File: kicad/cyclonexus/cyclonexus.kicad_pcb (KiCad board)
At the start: 2 copper layers, 92.7 x 111.8 mm, 22 parts, among them CON1 BARREL_JACK, CON2 BARREL_JACK, J1 RJ14, J10 RJ14, J11 RJ14, J12 RJ14, J13 RJ14, J14 RJ14, J15 RJ14, J16 RJ14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

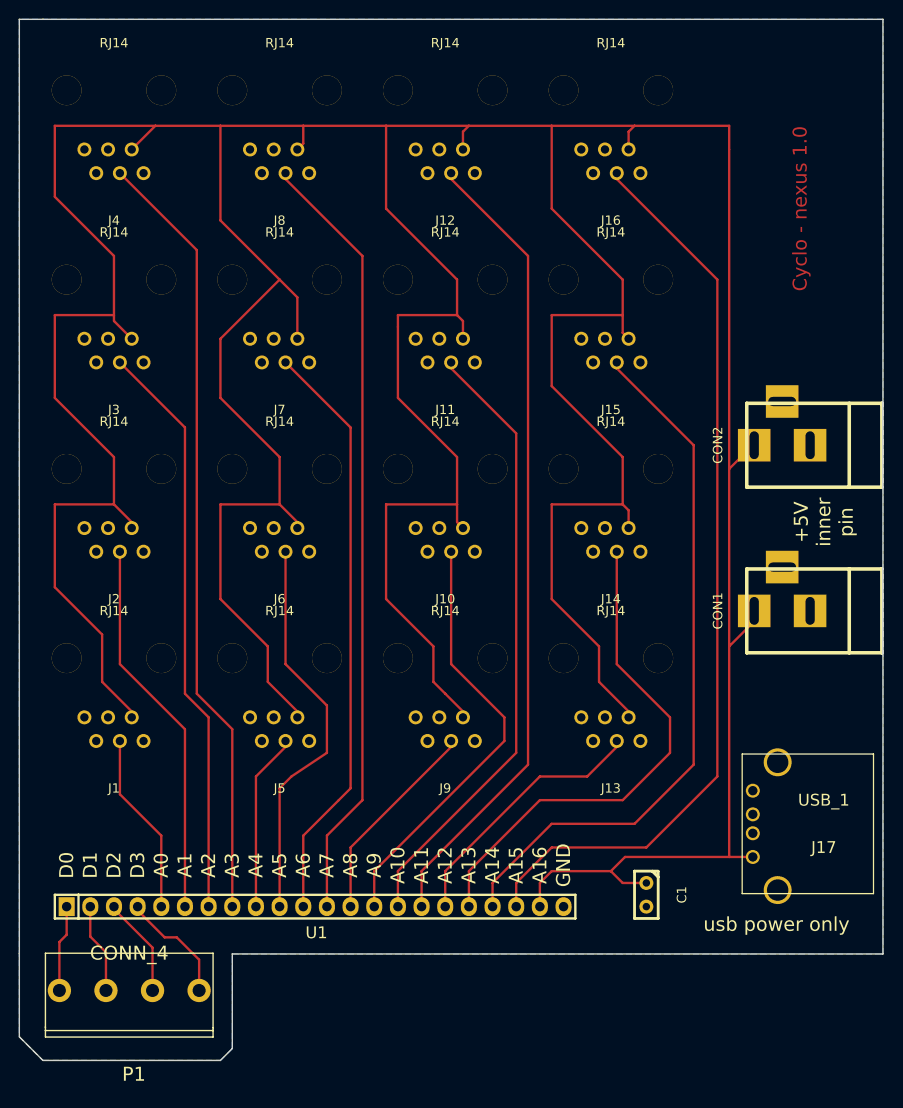
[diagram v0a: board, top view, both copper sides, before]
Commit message: add mounting holes
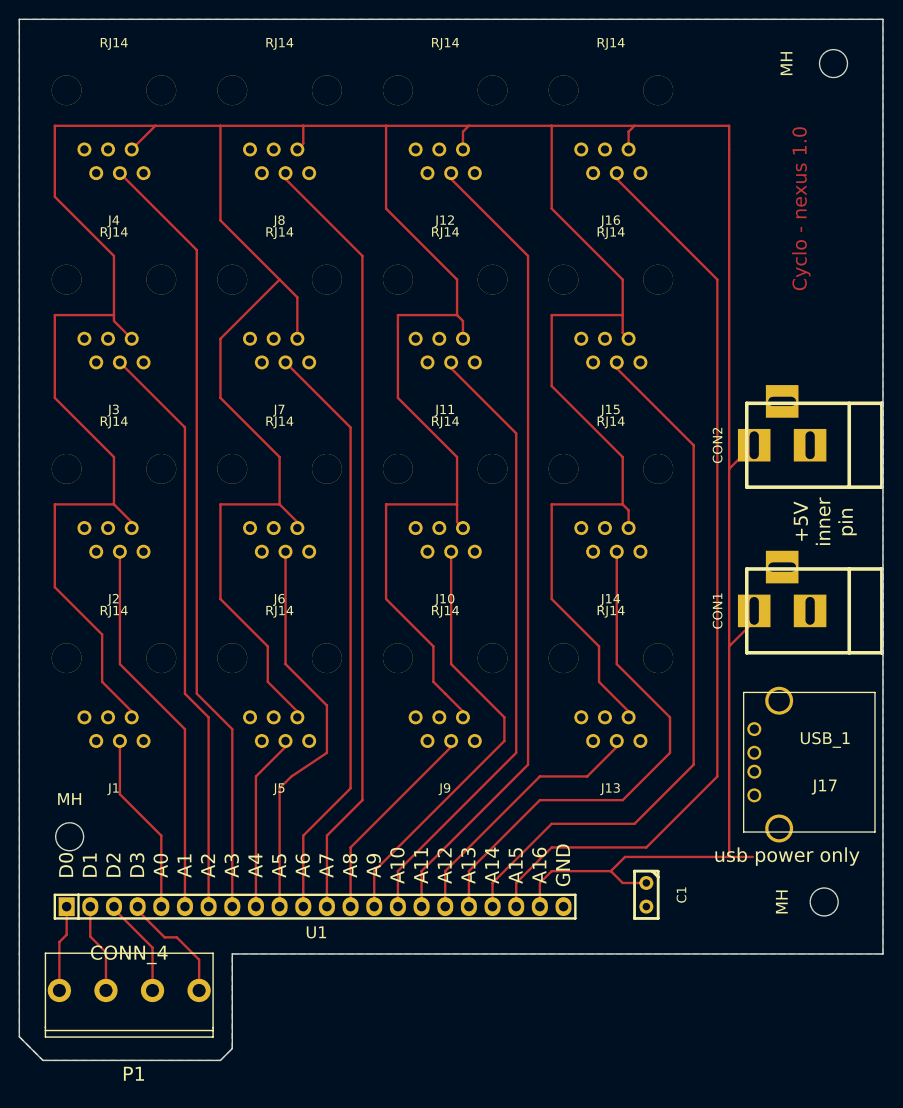
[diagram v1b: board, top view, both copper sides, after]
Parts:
- added MH: MountingHole_3mm_RevA_Date21Jun2010, Mounting_Holes:MountingHole_3mm, F.Cu at (107.0, 119.5)
- added MH: MountingHole_3mm_RevA_Date21Jun2010, Mounting_Holes:MountingHole_3mm, F.Cu at (189.0, 36.5)
- added MH: MountingHole_3mm_RevA_Date21Jun2010, Mounting_Holes:MountingHole_3mm, F.Cu at (188.0, 126.5)
- moved J17 6.61 mm to (180.5, 111.5)

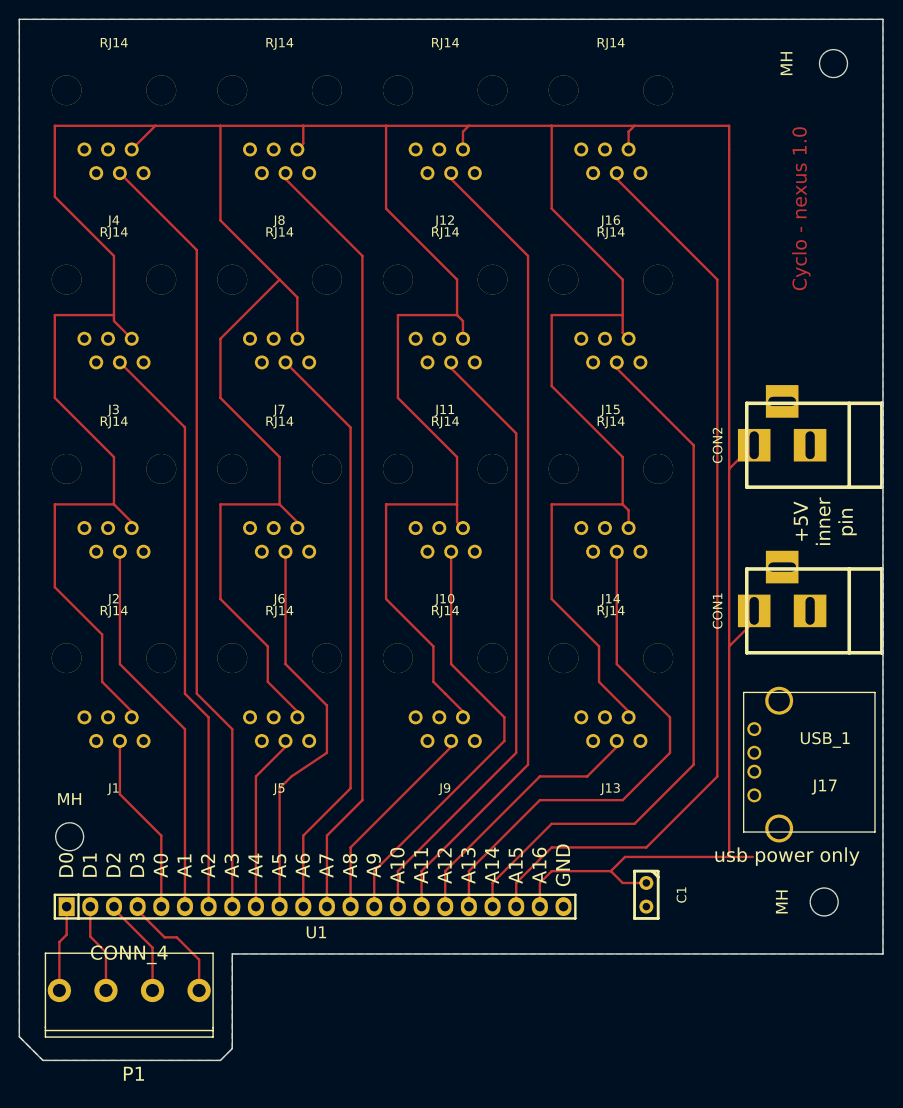
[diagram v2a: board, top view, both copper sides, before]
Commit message: redo of adc board with thicker traces, caps next to adc chips.
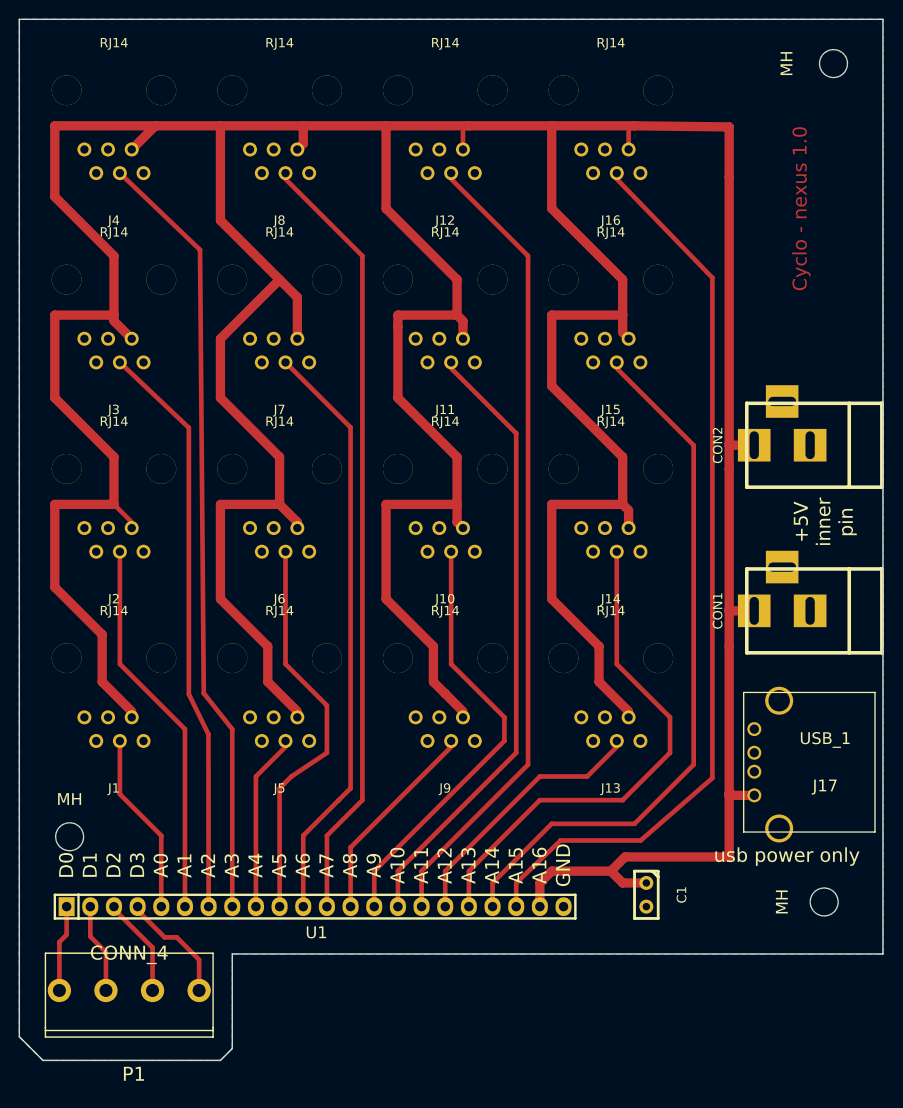
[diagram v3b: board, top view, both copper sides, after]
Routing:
- net A15: track 98.1 -> 97.0 mm
- net +5V: track 572.0 -> 570.9 mm
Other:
- net class fatty added: clearance 0.254, trace_width 1, via_dia 0.889, via_drill 0.635
- net class medium added: clearance 0.254, trace_width 0.5, via_dia 0.889, via_drill 0.635

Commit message: last changes before gerbers and ordering.
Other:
- board text added: "Cyclo Nexus 1.0"
- board text removed: "Cyclo - nexus 1.0"
